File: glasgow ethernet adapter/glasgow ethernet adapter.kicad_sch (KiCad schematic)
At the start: 44 parts, among them J1 Glasgow Port, J2 RJ45_Amphenol_RJMG201K21120FR, U1 MxL86110, Y1 25 MHz

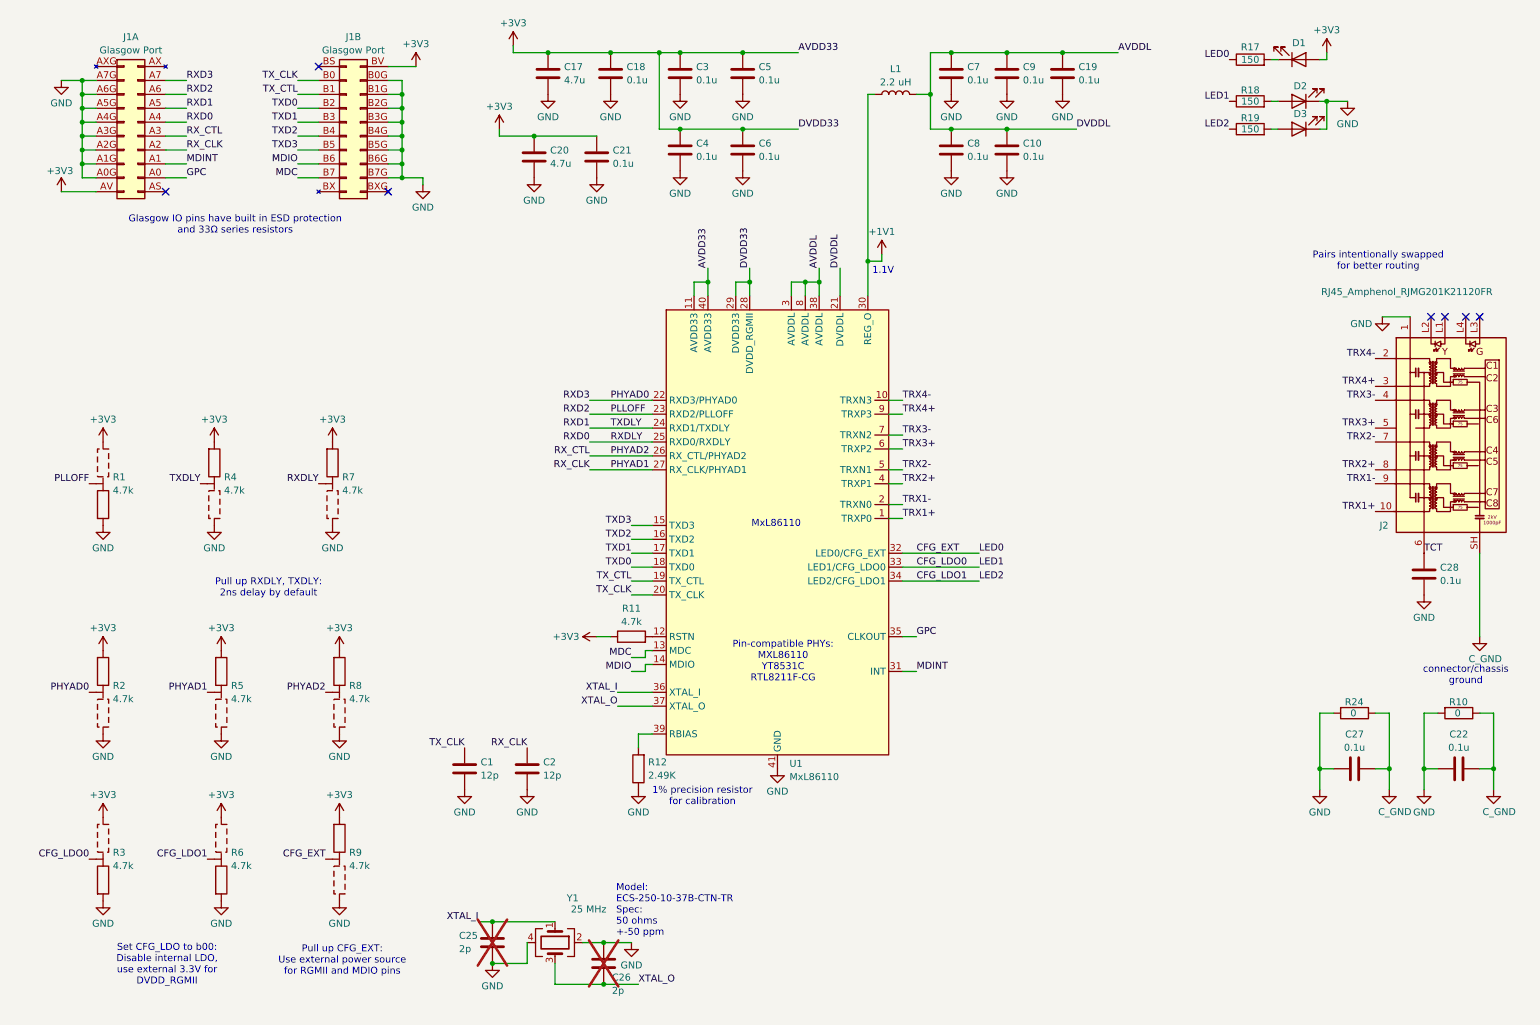
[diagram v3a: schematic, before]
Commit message: squash back to 2 layers
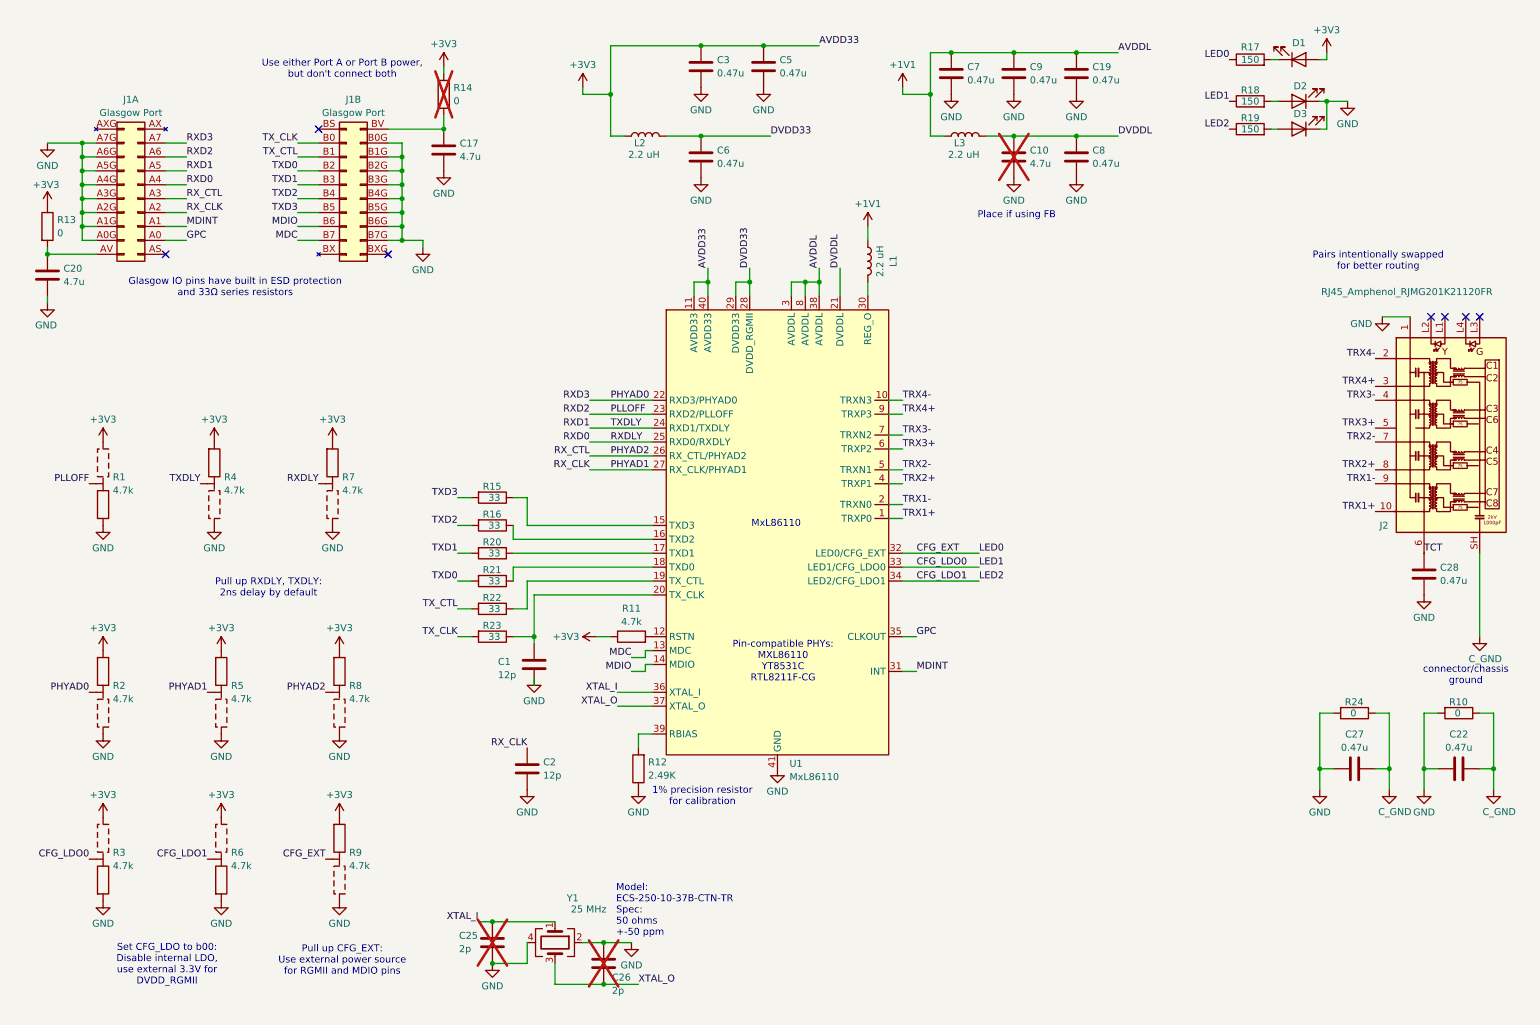
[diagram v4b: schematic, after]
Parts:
- removed C18, C21, C4: 0.1u, Capacitor_SMD:C_0402_1005Metric, symbol Device:C
- added L2, L3: 2.2 uH, Inductor_SMD:L_0603_1608Metric, symbol Device:L
- added R13, R14: 0, Resistor_SMD:R_0402_1005Metric, symbol Device:R
- added R15, R16, R20, R21, R22, R23: 33, Resistor_SMD:R_0402_1005Metric, symbol Device:R
- C10: value 0.1u -> 4.7u; footprint Capacitor_SMD:C_0402_1005Metric -> Capacitor_SMD:C_1206_3216Metric; now not fitted
- C19, C22, C27, C28, C3, C5, C6, C7, C8, C9: value 0.1u -> 0.47u
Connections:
- net +1V1: now also C19.1, C7.1, C9.1, U1.3 (AVDDL), U1.38 (AVDDL), U1.8 (AVDDL), L3.1; no longer U1.30 (REG_O)
- net +3V3: now also L2.1, R13.1, R14.2; no longer C17.1, C20.1, C6.1, J1.AV, J1.BV, U1.28 (DVDD_RGMII), U1.29 (DVDD33)
- net TXD0: now also R21.2; no longer U1.18 (TXD0)
- net TXD1: now also R20.2; no longer U1.17 (TXD1)
- net TXD2: now also R16.2; no longer U1.16 (TXD2)
- net TXD3: now also R15.2; no longer U1.15 (TXD3)
- net TX_CLK: now also R23.2; no longer C1.1, U1.20 (TX_CLK)
- net TX_CTL: now also R22.2; no longer U1.19 (TX_CTL)
- removed net AVDDL: C10.1, C19.1, C7.1, C8.1, C9.1, L1.2, U1.21 (DVDDL), U1.3 (AVDDL), U1.38 (AVDDL), U1.8 (AVDDL)
- new net: C17.1, J1.BV, R14.1
- new net: C20.1, J1.AV, R13.2
- new net: R15.1, U1.15 (TXD3)
- new net: R16.1, U1.16 (TXD2)
- new net: R20.1, U1.17 (TXD1)
- new net: R21.1, U1.18 (TXD0)
- new net: R22.1, U1.19 (TX_CTL)
- new net: C1.1, R23.1, U1.20 (TX_CLK)
- new net: L1.2, U1.30 (REG_O)
- new net DVDD33: C6.1, L2.2, U1.28 (DVDD_RGMII), U1.29 (DVDD33)
- new net DVDDL: C10.1, C8.1, L3.2, U1.21 (DVDDL)
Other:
- note added: "Place if using FB"
- note added: "Use either Port A or Port B power, but don't connect both"
- note removed: "1.1V"
- moved on the sheet: C1, C17, C19, C20, C3, C5, C6, C8, C9, J1A, J1B, L1

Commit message: add oscillator compatible layout
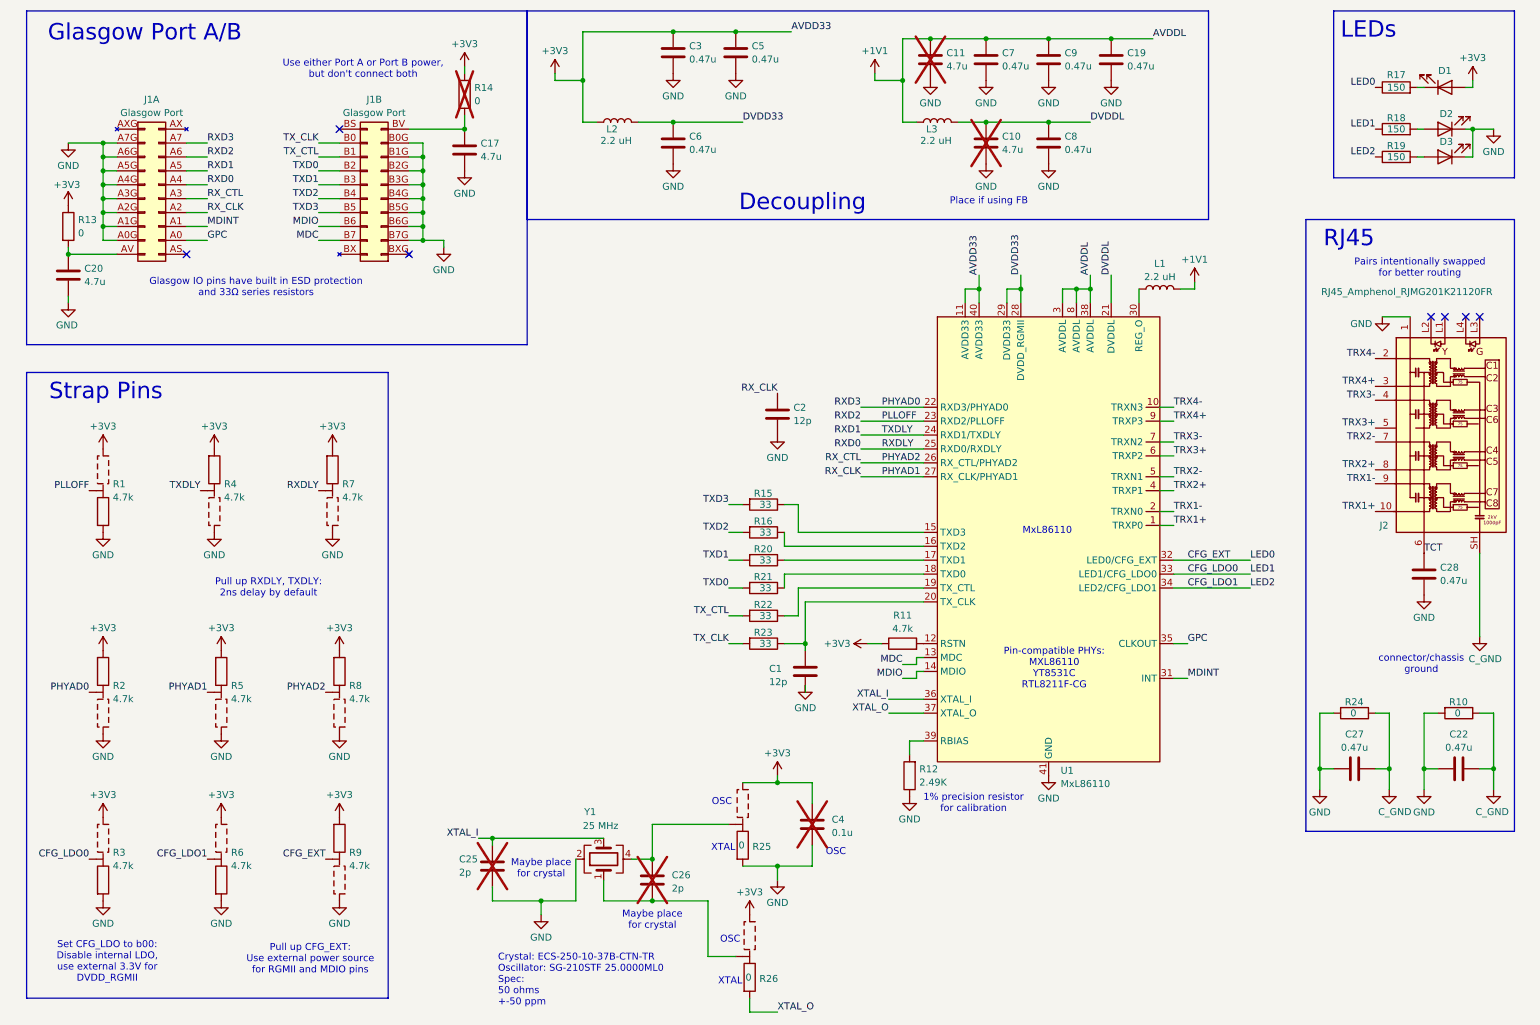
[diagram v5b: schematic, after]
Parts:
- added C11: 4.7u, Capacitor_SMD:C_1206_3216Metric, symbol Device:C
- added C4: 0.1u, Capacitor_SMD:C_0402_1005Metric, symbol Device:C
- added R25, R26: 0, glasgow:R-3-Way_0402_1005Metric, symbol glasgow:R-3-way
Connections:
- net +1V1: now also L1.2, C11.1; no longer L1.1
- net +3V3: now also C4.1, R25.3, R26.3
- net GND: now also C11.2, C4.2, R25.1; no longer C26.1, Y1.4
- net XTAL_I: now also Y1.3; no longer Y1.1
- net XTAL_O: now also R26.1; no longer C26.2, Y1.3
- net at U1.30 (REG_O): now also L1.1; no longer L1.2
- new net: C26.2, R26.2, Y1.1
- new net: C26.1, R25.2, Y1.4
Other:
- note added: "Crystal: ECS-250-10-37B-CTN-TR Oscillator: SG-210STF 25.0000ML0 Spec: 50 ohms +-50 ppm"
- note added: "Decoupling"
- note added: "Glasgow Port A/B"
- note added: "LEDs"
- note added: "Maybe place for crystal"
- note added: "OSC"
- note added: "RJ45"
- note added: "Strap Pins"
- note added: "XTAL"
- note removed: "Model: ECS-250-10-37B-CTN-TR Spec: 50 ohms +-50 ppm"
- moved on the sheet: C1, C10, C17, C19, C2, C20, C25, C26, C3, C5, C6, C7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

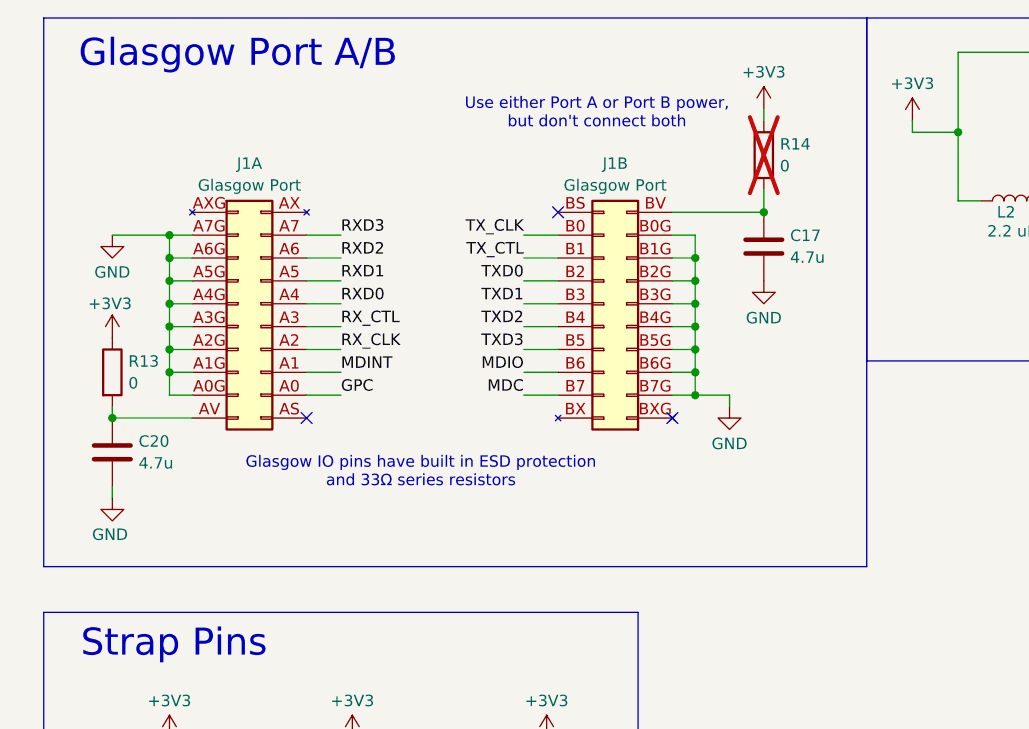
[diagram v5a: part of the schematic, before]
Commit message: go back to 4 layers
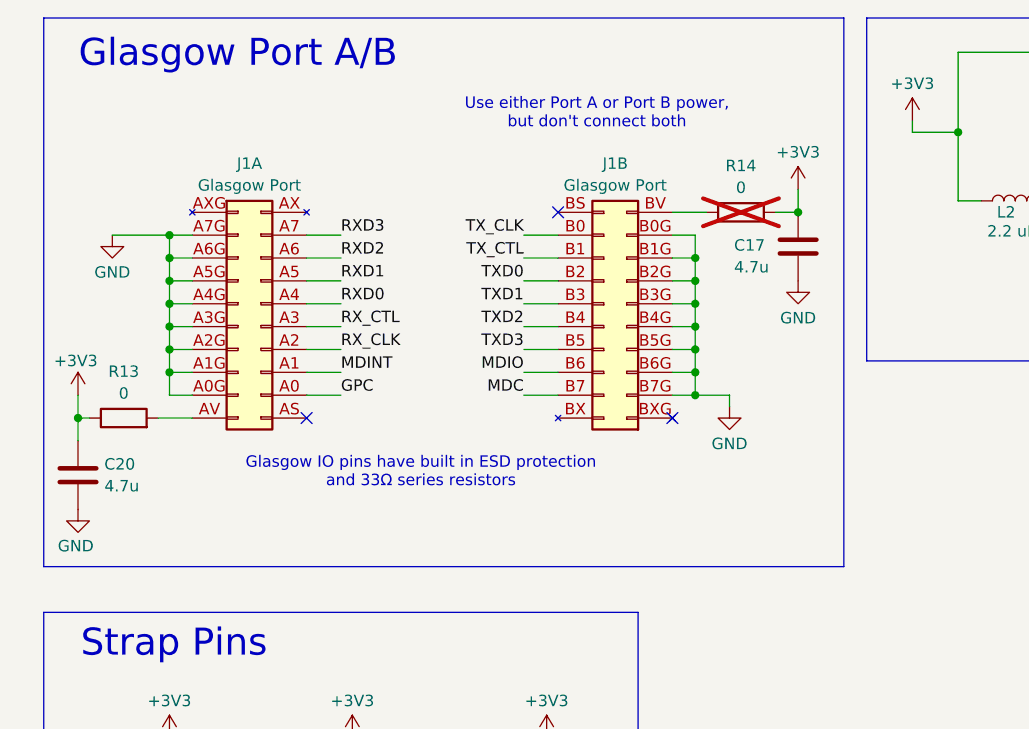
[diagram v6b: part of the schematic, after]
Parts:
- R13, R14: footprint Resistor_SMD:R_0402_1005Metric -> Resistor_SMD:R_0603_1608Metric
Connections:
- net +3V3: now also C17.1, C20.1, R14.1; no longer R14.2
- net at J1.AV, R13.2: no longer C20.1
- new net: J1.BV, R14.2
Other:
- moved on the sheet: C17, C20, R13, R14
